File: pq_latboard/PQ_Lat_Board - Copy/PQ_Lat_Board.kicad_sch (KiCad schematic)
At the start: 27 parts, among them IC1 TCN75AVOA713, J1 Conn_01x11_MountingPin, J2 Conn_Coaxial

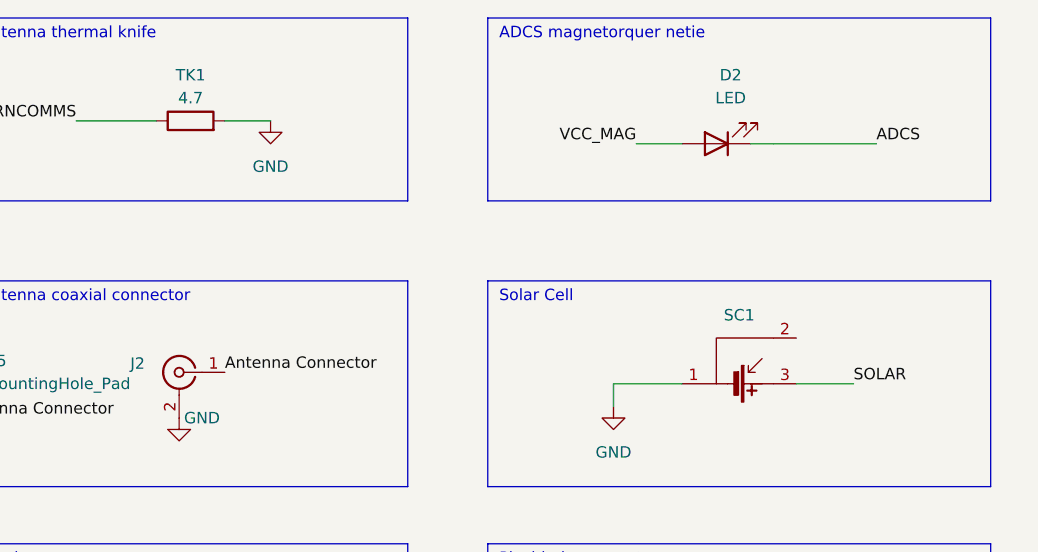
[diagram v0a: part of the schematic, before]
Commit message: lateral fixed
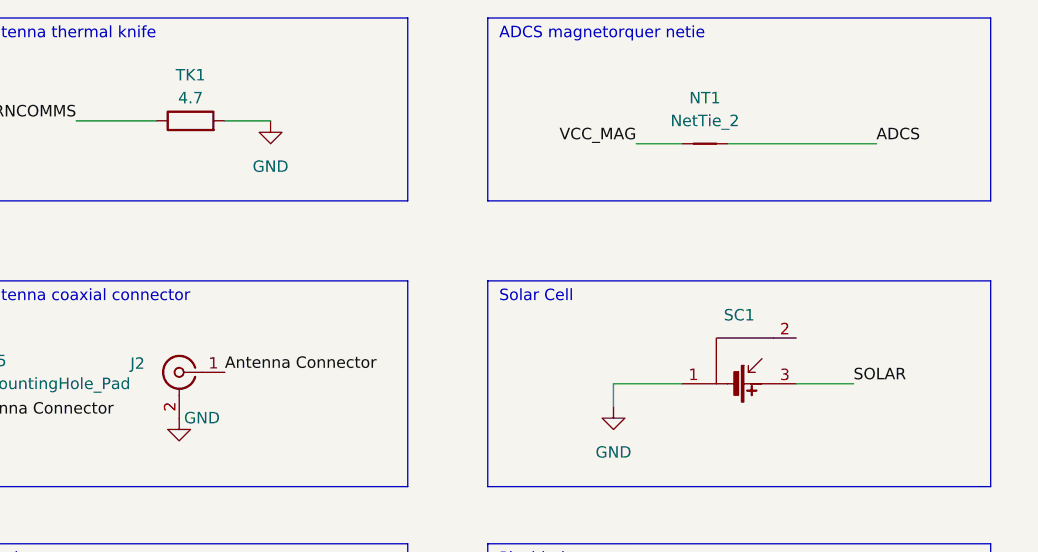
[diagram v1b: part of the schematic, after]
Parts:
- removed D2: LED, LED_SMD:LED_0402_1005Metric, symbol Device:LED
- added NT1: NetTie_2, NetTie:NetTie-2_SMD_Pad0.5mm, symbol Device:NetTie_2
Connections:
- net ADCS: now also NT1.2
- net VCC_MAG: now also NT1.1
